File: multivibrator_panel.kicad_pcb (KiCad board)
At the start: 2 copper layers, 98 x 98 mm, 208 parts, among them J1 Conn_01x02_Pin, Q1 2SC1815, Q2 2SC1815

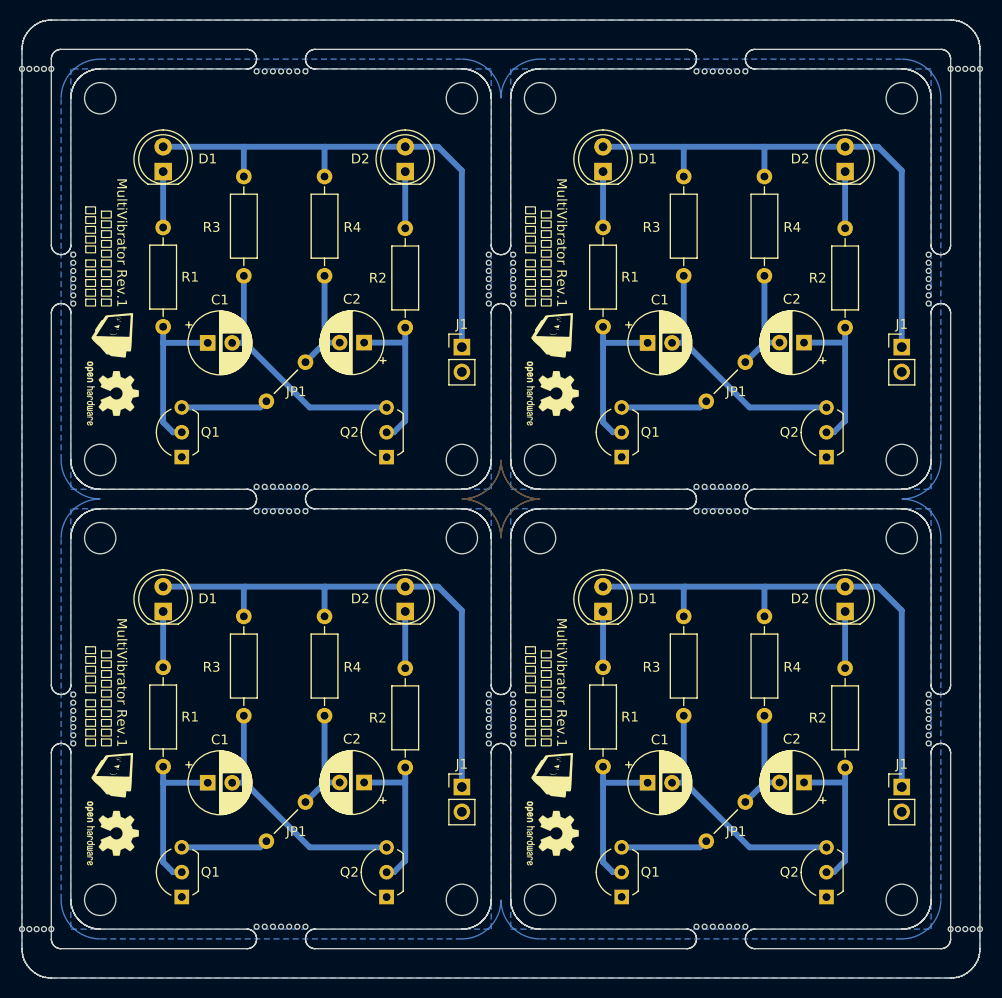
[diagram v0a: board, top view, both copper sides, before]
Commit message: chore: panelize
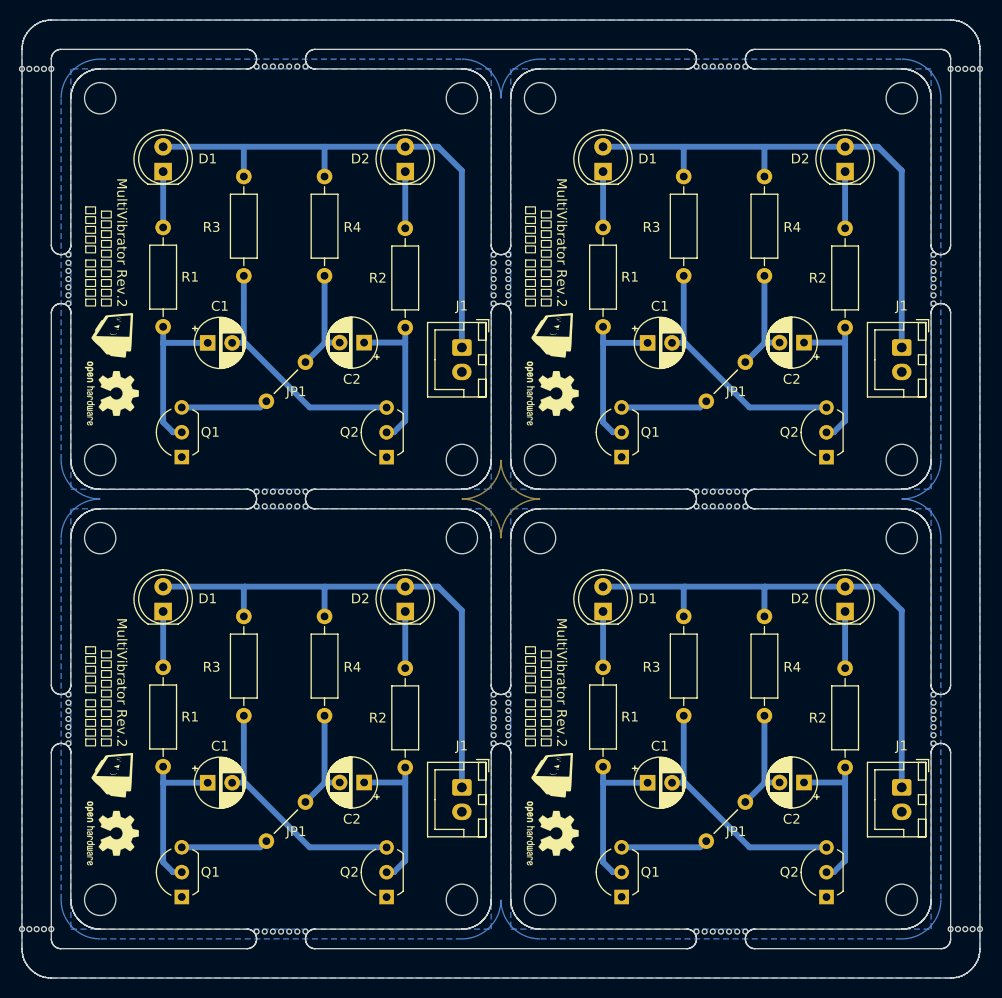
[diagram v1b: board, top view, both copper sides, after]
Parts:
- removed the C1 at (118.5, 53.0)
- removed the C1 at (163.5, 98.0)
- removed the C1 at (118.5, 98.0)
- removed the C1 at (163.5, 53.0)
- removed the C2 at (179.5, 53.0)
- removed the C2 at (134.5, 98.0)
- removed the C2 at (134.5, 53.0)
- removed the C2 at (179.5, 98.0)
- removed the J1 at (189.5, 98.5)
- removed the J1 at (189.5, 53.5)
- removed the J1 at (144.5, 98.5)
- removed the J1 at (144.5, 53.5)
- added C1: 100u, Capacitor_THT:CP_Radial_D5.0mm_P2.50mm, F.Cu at (163.5, 98.0)
- added C1: 100u, Capacitor_THT:CP_Radial_D5.0mm_P2.50mm, F.Cu at (118.5, 98.0)
- added C1: 100u, Capacitor_THT:CP_Radial_D5.0mm_P2.50mm, F.Cu at (118.5, 53.0)
- added C1: 100u, Capacitor_THT:CP_Radial_D5.0mm_P2.50mm, F.Cu at (163.5, 53.0)
- added C2: 100u, Capacitor_THT:CP_Radial_D5.0mm_P2.50mm, F.Cu at (134.5, 53.0)
- added C2: 100u, Capacitor_THT:CP_Radial_D5.0mm_P2.50mm, F.Cu at (134.5, 98.0)
- added C2: 100u, Capacitor_THT:CP_Radial_D5.0mm_P2.50mm, F.Cu at (179.5, 98.0)
- added C2: 100u, Capacitor_THT:CP_Radial_D5.0mm_P2.50mm, F.Cu at (179.5, 53.0)
- added J1: Conn_01x02_Pin, Connector_JST:JST_XH_B2B-XH-A_1x02_P2.50mm_Vertical, F.Cu at (189.5, 98.5)
- added J1: Conn_01x02_Pin, Connector_JST:JST_XH_B2B-XH-A_1x02_P2.50mm_Vertical, F.Cu at (144.5, 98.5)
- added J1: Conn_01x02_Pin, Connector_JST:JST_XH_B2B-XH-A_1x02_P2.50mm_Vertical, F.Cu at (144.5, 53.5)
- added J1: Conn_01x02_Pin, Connector_JST:JST_XH_B2B-XH-A_1x02_P2.50mm_Vertical, F.Cu at (189.5, 53.5)
- moved KiKit_MB_10_1 0.50 mm to (147.8, 89.0)
- moved KiKit_MB_10_2 0.50 mm to (147.8, 89.8)
- moved KiKit_MB_10_3 0.50 mm to (147.8, 90.7)
- moved KiKit_MB_10_4 0.50 mm to (147.8, 91.5)
- moved KiKit_MB_10_5 0.50 mm to (147.8, 92.3)
- moved KiKit_MB_10_6 0.50 mm to (147.8, 93.2)
- moved KiKit_MB_10_7 0.50 mm to (147.8, 94.0)
- moved KiKit_MB_11_1 0.50 mm to (123.5, 69.8)
- moved KiKit_MB_11_2 0.50 mm to (124.3, 69.8)
- moved KiKit_MB_11_3 0.50 mm to (125.2, 69.8)
- moved KiKit_MB_11_4 0.50 mm to (126.0, 69.8)
- moved KiKit_MB_11_5 0.50 mm to (126.8, 69.8)
- moved KiKit_MB_11_6 0.50 mm to (127.7, 69.8)
- moved KiKit_MB_11_7 0.50 mm to (128.5, 69.8)
- moved KiKit_MB_12_1 0.50 mm to (128.5, 113.2)
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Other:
- board text added: "MultiVibrator Rev.2 本郷中学校・高等学校 マイコン部 電子工作班"
- board text removed: "MultiVibrator Rev.1 本郷中学校・高等学校 マイコン部 電子工作班"

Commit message: chore: panelize and generate gerber
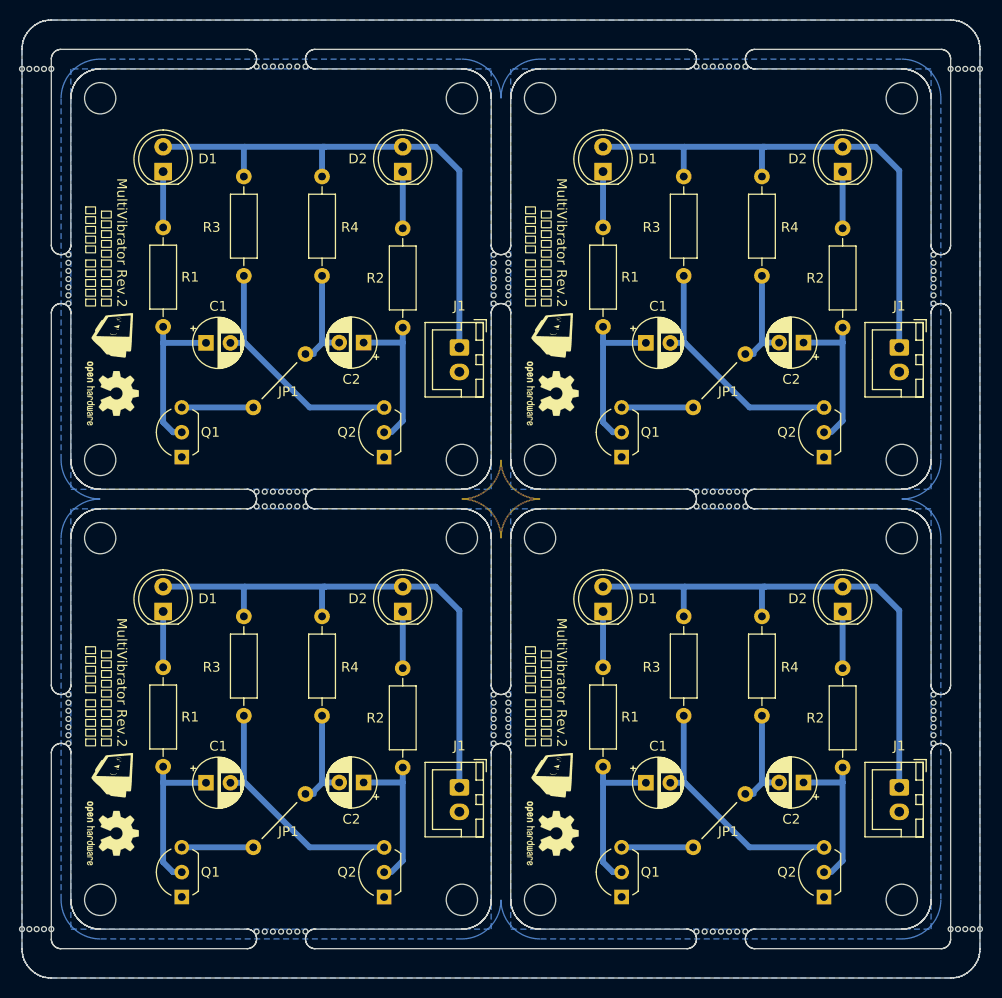
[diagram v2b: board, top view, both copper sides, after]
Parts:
- removed the ? at (173.5, 100.0)
- removed the ? at (128.5, 55.0)
- removed the ? at (124.5, 104.0)
- removed the ? at (128.5, 100.0)
- removed the ? at (169.5, 59.0)
- removed the ? at (173.5, 55.0)
- removed the ? at (169.5, 104.0)
- removed the ? at (124.5, 59.0)
- removed the C1 at (163.5, 98.0)
- removed the C1 at (118.5, 98.0)
- removed the C1 at (118.5, 53.0)
- removed the C1 at (163.5, 53.0)
- removed the C2 at (134.5, 53.0)
- removed the C2 at (134.5, 98.0)
- removed the C2 at (179.5, 98.0)
- removed the C2 at (179.5, 53.0)
- removed the D2 at (183.7, 35.5)
- removed the D2 at (138.7, 35.5)
- removed the D2 at (183.7, 80.5)
- removed the D2 at (138.7, 80.5)
- removed the J1 at (189.5, 98.5)
- removed the J1 at (144.5, 98.5)
- removed the J1 at (144.5, 53.5)
- removed the J1 at (189.5, 53.5)
- removed the Q2 at (181.8, 109.7)
- removed the Q2 at (181.8, 64.7)
- removed the Q2 at (136.8, 64.7)
- removed the Q2 at (136.8, 109.7)
- removed the R2 at (138.7, 41.3)
- removed the R2 at (183.7, 41.3)
- removed the R2 at (183.7, 86.3)
- removed the R2 at (138.7, 86.3)
- removed the R4 at (175.4, 81.0)
- removed the R4 at (130.4, 36.0)
- removed the R4 at (175.4, 36.0)
- removed the R4 at (130.4, 81.0)
- added ?: , , F.Cu at (173.5, 54.2)
- added ?: , , F.Cu at (168.2, 104.6)
- added ?: , , F.Cu at (123.2, 59.6)
- added ?: , , F.Cu at (123.2, 104.6)
- added ?: , , F.Cu at (173.5, 99.2)
- added ?: , , F.Cu at (128.5, 54.2)
- added ?: , , F.Cu at (128.5, 99.2)
- added ?: , , F.Cu at (168.2, 59.6)
- added C1: 100u, Capacitor_THT:CP_Radial_D5.0mm_P2.50mm, F.Cu at (163.3, 53.0)
- added C1: 100u, Capacitor_THT:CP_Radial_D5.0mm_P2.50mm, F.Cu at (163.3, 98.0)
- added C1: 100u, Capacitor_THT:CP_Radial_D5.0mm_P2.50mm, F.Cu at (118.3, 98.0)
- added C1: 100u, Capacitor_THT:CP_Radial_D5.0mm_P2.50mm, F.Cu at (118.3, 53.0)
- added C2: 100u, Capacitor_THT:CP_Radial_D5.0mm_P2.50mm, F.Cu at (134.4, 53.0)
- added C2: 100u, Capacitor_THT:CP_Radial_D5.0mm_P2.50mm, F.Cu at (134.4, 98.0)
- added C2: 100u, Capacitor_THT:CP_Radial_D5.0mm_P2.50mm, F.Cu at (179.4, 53.0)
- added C2: 100u, Capacitor_THT:CP_Radial_D5.0mm_P2.50mm, F.Cu at (179.4, 98.0)
- added D2: LED, LED_THT:LED_D5.0mm, F.Cu at (138.5, 35.5)
- added D2: LED, LED_THT:LED_D5.0mm, F.Cu at (183.5, 35.5)
- added D2: LED, LED_THT:LED_D5.0mm, F.Cu at (183.5, 80.5)
- added D2: LED, LED_THT:LED_D5.0mm, F.Cu at (138.5, 80.5)
- added J1: Conn_01x02_Pin, Connector_JST:JST_XH_B2B-XH-A_1x02_P2.50mm_Vertical, F.Cu at (144.2, 98.5)
- added J1: Conn_01x02_Pin, Connector_JST:JST_XH_B2B-XH-A_1x02_P2.50mm_Vertical, F.Cu at (144.2, 53.5)
- added J1: Conn_01x02_Pin, Connector_JST:JST_XH_B2B-XH-A_1x02_P2.50mm_Vertical, F.Cu at (189.2, 53.5)
- added J1: Conn_01x02_Pin, Connector_JST:JST_XH_B2B-XH-A_1x02_P2.50mm_Vertical, F.Cu at (189.2, 98.5)
- added Q2: 2SC1815, Package_TO_SOT_THT:TO-92L_Inline_Wide, F.Cu at (136.5, 64.7)
- added Q2: 2SC1815, Package_TO_SOT_THT:TO-92L_Inline_Wide, F.Cu at (181.5, 109.7)
- added Q2: 2SC1815, Package_TO_SOT_THT:TO-92L_Inline_Wide, F.Cu at (181.5, 64.7)
- added Q2: 2SC1815, Package_TO_SOT_THT:TO-92L_Inline_Wide, F.Cu at (136.5, 109.7)
- added R2: 330, Resistor_THT:R_Axial_DIN0207_L6.3mm_D2.5mm_P10.16mm_Horizontal, F.Cu at (183.5, 41.3)
- added R2: 330, Resistor_THT:R_Axial_DIN0207_L6.3mm_D2.5mm_P10.16mm_Horizontal, F.Cu at (138.5, 41.3)
- added R2: 330, Resistor_THT:R_Axial_DIN0207_L6.3mm_D2.5mm_P10.16mm_Horizontal, F.Cu at (183.5, 86.3)
- added R2: 330, Resistor_THT:R_Axial_DIN0207_L6.3mm_D2.5mm_P10.16mm_Horizontal, F.Cu at (138.5, 86.3)
- added R4: 10k, Resistor_THT:R_Axial_DIN0207_L6.3mm_D2.5mm_P10.16mm_Horizontal, F.Cu at (175.2, 36.0)
- added R4: 10k, Resistor_THT:R_Axial_DIN0207_L6.3mm_D2.5mm_P10.16mm_Horizontal, F.Cu at (130.2, 36.0)
- added R4: 10k, Resistor_THT:R_Axial_DIN0207_L6.3mm_D2.5mm_P10.16mm_Horizontal, F.Cu at (130.2, 81.0)
- added R4: 10k, Resistor_THT:R_Axial_DIN0207_L6.3mm_D2.5mm_P10.16mm_Horizontal, F.Cu at (175.2, 81.0)
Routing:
- net Board_1-Net-(Q1-B): track 20.1 -> 18.2 mm
- net Board_0-Net-(Q1-B): track 20.1 -> 18.2 mm
- net Board_3-Net-(Q1-B): track 20.1 -> 18.2 mm
- net Board_2-Net-(Q1-B): track 20.1 -> 18.2 mm
- net Board_3-Net-(Q2-C): track 16.1 -> 15.4 mm
- net Board_2-Net-(Q2-C): track 16.1 -> 15.4 mm
- net Board_1-Net-(Q2-C): track 16.1 -> 15.4 mm
- net Board_0-Net-(Q2-C): track 16.1 -> 15.4 mm

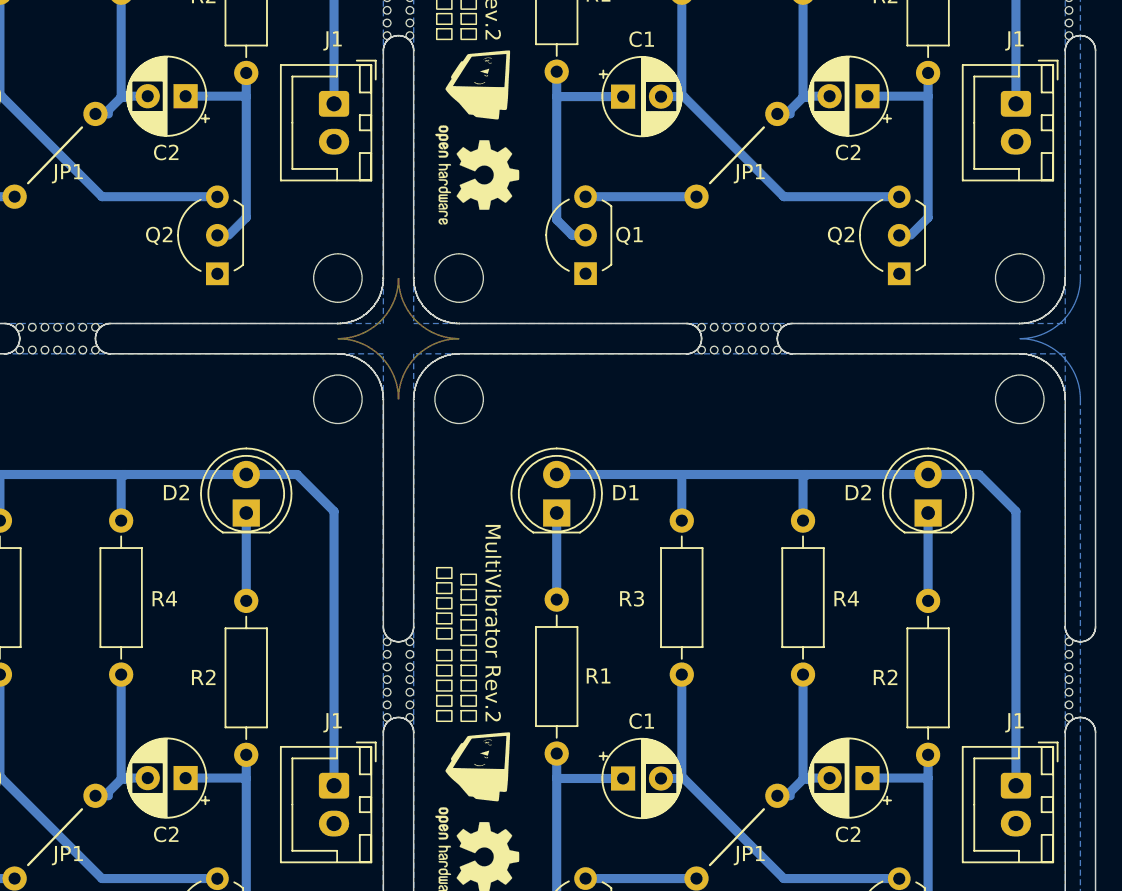
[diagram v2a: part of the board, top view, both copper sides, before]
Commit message: fix: resolve weird path and regenerate gerber
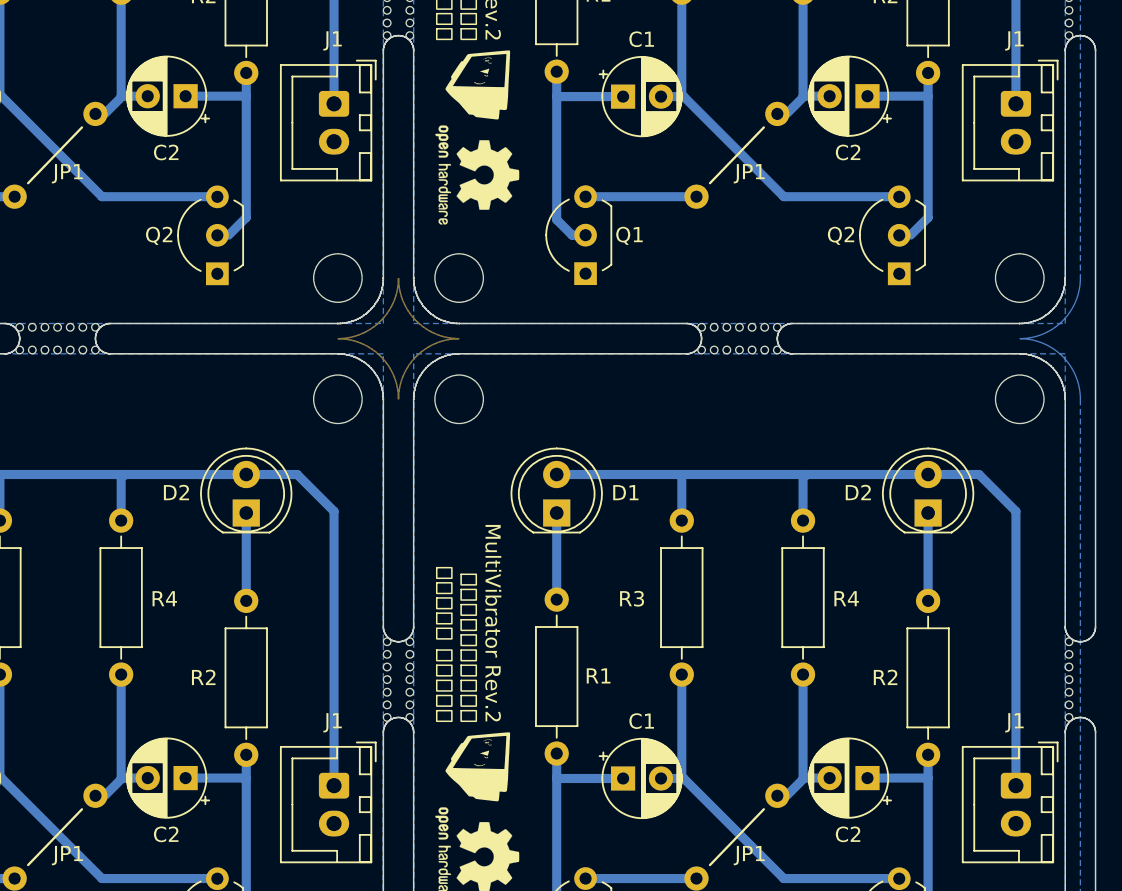
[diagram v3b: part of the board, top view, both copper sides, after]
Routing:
- net Board_3-Net-(Q1-B): track 18.2 -> 17.5 mm
- net Board_2-Net-(Q1-B): track 18.2 -> 17.5 mm
- net Board_0-Net-(Q1-B): track 18.2 -> 17.5 mm
- net Board_1-Net-(Q1-B): track 18.2 -> 17.5 mm
